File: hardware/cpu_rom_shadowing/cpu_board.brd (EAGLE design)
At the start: 167.9 x 122.5 mm, 53 parts, among them IC4 7404N, IC5 7400N, IC6 74HCT139N, IC7 7400N, IC9 74HCT138N, X1 22-23-2041

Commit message: ROM shadowed version of PCB modified
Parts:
- removed C15: 100n, rcl:C1206
- removed C5: 100n, rcl:C0603
- removed IC4: 7404N, 74xx-us:DIL14
- removed IC7: 7400N, 74xx-eu:DIL14
- IC5: value 7400N -> 74HCT08N
- moved C16 100.0 mm to (16.8, 107.7)
- moved IC5 92.7 mm to (118.7, 13.3), turned to 270 degrees
- moved C12 3.82 mm to (106.7, 23.5)
- moved IC6 3.19 mm to (99.7, 14.6)
- moved C17 1.27 mm to (78.7, 92.7)
- moved Q1 1.27 mm to (75.6, 94.0)
- moved C13 0.63 mm to (143.2, 23.5)
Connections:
- removed net A14_SWITCH: IC5.6, U$5.20
- removed net A15_SWITCH: IC5.3, U$5.7
- removed net BANK_A14: IC7.6, U$2.1
- removed net CS_BANKED_RAM: IC6.12, U$2.20
- removed net CS_RAM: IC6.4, U$4.20
- removed net N$19: IC6.15, IC6.5
- removed net N$20: IC9.6, R9.1
- removed net N$21: IC5.5, IC5.8
- removed net N$26: IC5.1, IC5.11
- removed net START_MEM_SWITCH: IC5.2, IC5.4, U$1.8
- new net CS_RAM1: IC6.10, U$4.20
- new net CS_RAM2: IC5.6, U$2.20
- new net N$2: IC5.4, IC6.11
- new net N$8: IC5.5, IC6.9
- new net PULLUP_5V: IC5.10, IC5.12, IC9.6, R9.1
- new net SHADOW_ROM: IC6.14, U$1.8
- net !CS_PORT_OUT: now also IC5.8; no longer IC4.8
- net !RESET: now also IC5.11; no longer IC4.4
- net 8275_DACK: no longer IC7.4
- net A14: now also U$2.1; no longer IC6.14
- net A14_CPU: now also U$5.20; no longer IC5.10, IC5.9
- net A15: now also IC6.13; no longer IC6.2
- net A15_CPU: now also U$5.7; no longer IC5.12, IC5.13
- net CS_EPROM: now also IC6.12; no longer IC6.11
- net CS_PORT_OUT: now also IC5.9; no longer IC4.9
- net GND: now also IC5.1, IC5.2, IC6.15, IC6.2; no longer C15.2, C5.2, IC4.1, IC4.11, IC4.13, IC4.5, IC4.7, IC6.13, IC7.1, IC7.10, IC7.12, IC7.13, IC7.2, IC7.7, IC7.9
- net RESET: now also IC5.13; no longer IC4.3
- net SET_BANK_A14: no longer IC7.5
- net VCC: no longer C15.1, C5.1, IC4.14, IC7.14
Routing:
- net START_MEM_SWITCH: track 188.3 -> 0.00 mm, vias 4 -> 0
- net VCC: track 624.8 -> 527.3 mm
- net SHADOW_ROM: track 0.00 -> 96.6 mm, vias 0 -> 2
- net BANK_A14: track 88.4 -> 0.00 mm, vias 4 -> 0
- net CS_RAM1: track 0.00 -> 87.4 mm, vias 0 -> 2
- net CS_BANKED_RAM: track 85.8 -> 0.00 mm, vias 2 -> 0
- net CS_RAM2: track 0.00 -> 79.3 mm, vias 0 -> 2
- net CS_RAM: track 76.4 -> 0.00 mm, vias 2 -> 0
- net A15_SWITCH: track 63.2 -> 0.00 mm, vias 2 -> 0
- net A14_SWITCH: track 55.0 -> 0.00 mm, vias 2 -> 0
- net A15_CPU: track 86.3 -> 37.2 mm, vias 2 -> 0
- net SET_BANK_A14: track 46.0 -> 0.00 mm, vias 2 -> 0
- net 8275_DACK: track 43.4 -> 0.00 mm
- net A14_CPU: track 45.7 -> 9.41 mm, vias 2 -> 0
- net PULLUP_5V: track 0.00 -> 31.1 mm
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
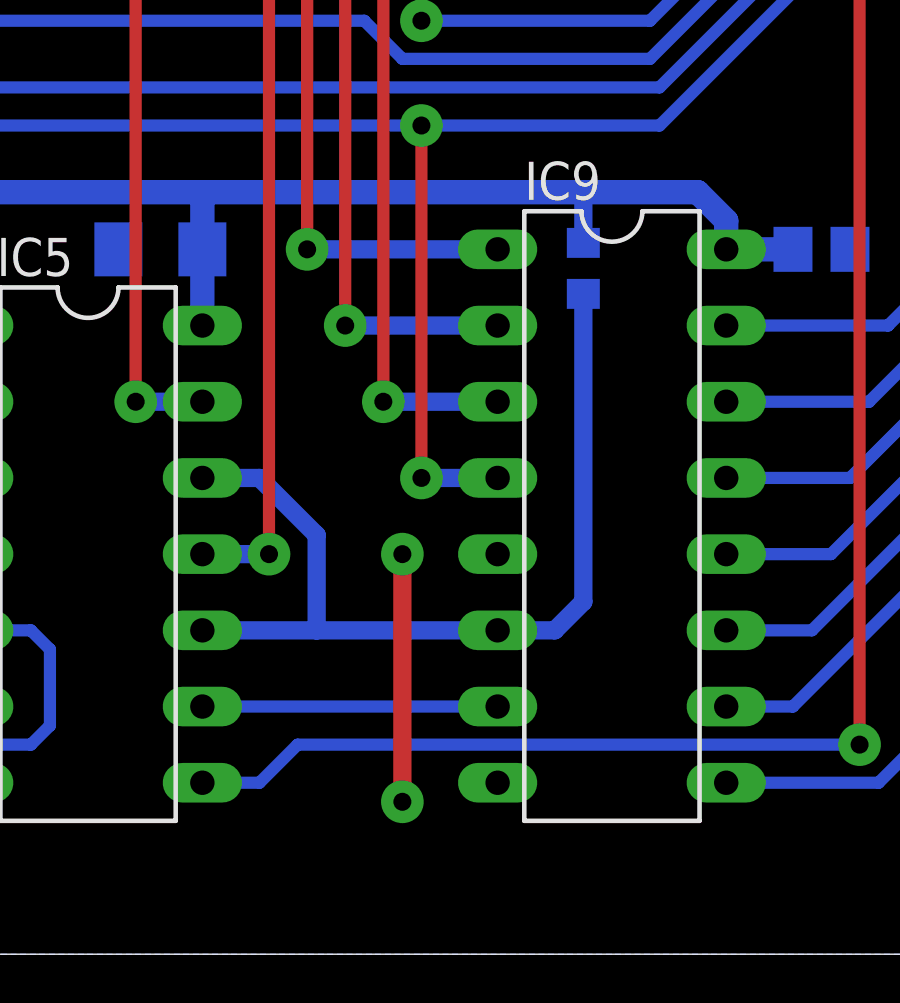
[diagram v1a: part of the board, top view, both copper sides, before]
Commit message: Isolate pramaeter changeg in CPU board
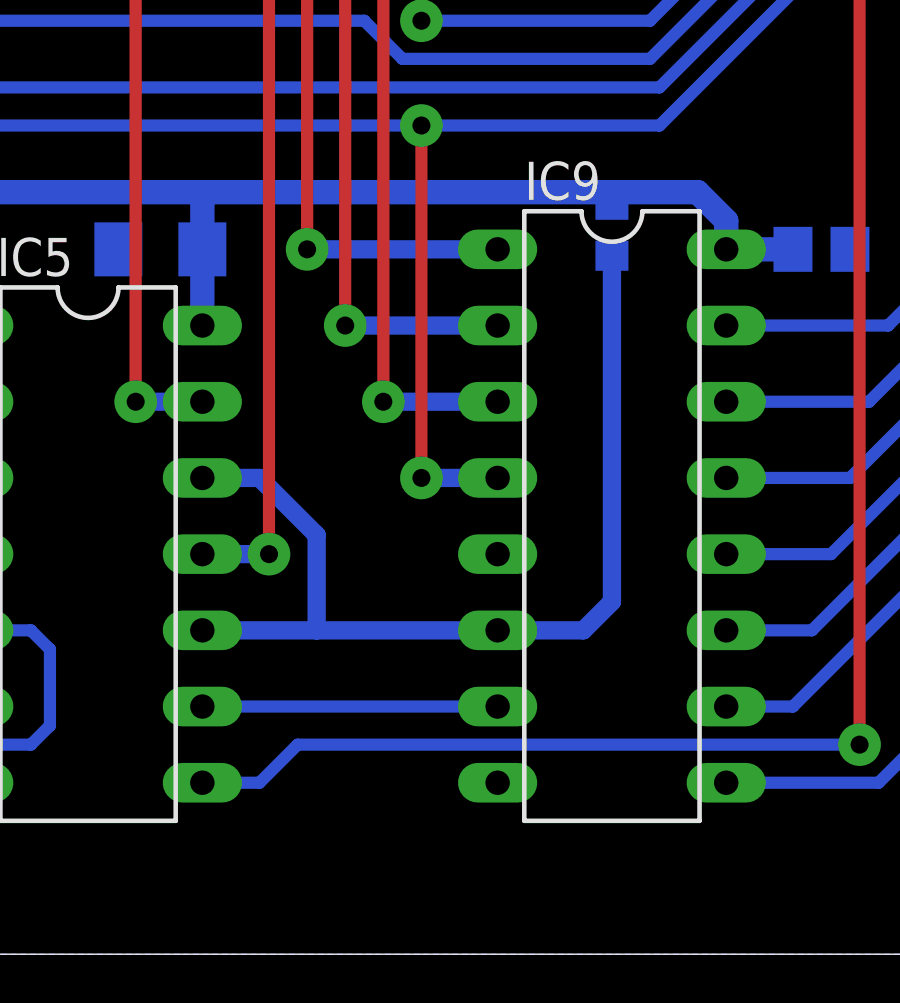
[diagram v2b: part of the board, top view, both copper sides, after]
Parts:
- moved R9 1.59 mm to (136.2, 24.1)
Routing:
- net GND: track 143.0 -> 134.8 mm, vias 18 -> 16
- net PULLUP_5V: track 31.1 -> 33.4 mm
- net VCC: track 527.3 -> 526.0 mm
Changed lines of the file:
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@@
 <element name="C9" library="rcl" package="C1206" value="100n" x="100.965" y="117.6147" rot="MR90"/>
 <element name="IC6" library="74xx-eu" package="DIL16" value="74HCT139N" x="99.695" y="14.605" rot="R270"/>
-<element name="R9" library="rcl" package="R0603" value="10k" x="135.255" y="22.86" rot="MR90"/>
+<element name="R9" library="rcl" package="R0603" value="10k" x="136.2075" y="24.13" rot="MR90"/>
 <element name="C10" library="rcl" package="E5-10,5" value="" x="134.62" y="113.665" rot="R270"/>
 <element name="C11" library="rcl" package="C0805" value="100n" x="48.5775" y="111.4425" rot="MR90"/>
@@
 <wire x1="93.345" y1="25.4" x2="103.505" y2="25.4" width="0.8128" layer="16"/>
 <wire x1="103.505" y1="25.4" x2="122.555" y2="25.4" width="0.8128" layer="16"/>
-<wire x1="122.555" y1="25.4" x2="135.255" y2="25.4" width="0.8128" layer="16"/>
-<wire x1="135.255" y1="25.4" x2="139.065" y2="25.4" width="0.8128" layer="16"/>
+<wire x1="122.555" y1="25.4" x2="136.2075" y2="25.4" width="0.8128" layer="16"/>
+<wire x1="136.2075" y1="25.4" x2="139.065" y2="25.4" width="0.8128" layer="16"/>
 <wire x1="139.065" y1="25.4" x2="140.0175" y2="24.4475" width="0.8128" layer="16"/>
 <wire x1="140.0175" y1="24.4475" x2="140.0175" y2="23.495" width="0.8128" layer="16"/>
-<wire x1="135.255" y1="23.71" x2="135.255" y2="25.4" width="0.6096" layer="16"/>
+<wire x1="136.2075" y1="24.98" x2="136.2075" y2="25.4" width="0.6096" layer="16"/>
 <wire x1="10.795" y1="71.755" x2="13.97" y2="71.755" width="0.6096" layer="16"/>
 <wire x1="13.97" y1="71.755" x2="18.7325" y2="71.755" width="0.6096" layer="16"/>
@@
 <wire x1="118.6434" y1="45.4884" x2="118.745" y2="45.4376" width="1.016" layer="16"/>
 <wire x1="118.7196" y1="45.463" x2="118.745" y2="45.4376" width="1.016" layer="16"/>
-<polygon width="0.4064" layer="16" isolate="0.6096" thermals="no">
+<polygon width="0.4064" layer="16" isolate="0.4064" thermals="no">
 <vertex x="0" y="122.555"/>
 <vertex x="0" y="0"/>
@@
 <contactref element="IC6" pad="3"/>
 <contactref element="IC6" pad="1"/>
-<via x="129.2225" y="13.335" extent="1-16" drill="0.6" diameter="1.4224" shape="octagon"/>
-<via x="129.2225" y="5.08" extent="1-16" drill="0.6" diameter="1.4224" shape="octagon"/>
-<wire x1="129.2225" y1="13.335" x2="129.2225" y2="5.08" width="0.6096" layer="1"/>
 <contactref element="IC5" pad="1"/>
 <contactref element="IC5" pad="2"/>
@@
 <contactref element="IC9" pad="6"/>
 <contactref element="R9" pad="1"/>
-<wire x1="135.255" y1="22.01" x2="135.255" y2="11.7475" width="0.6096" layer="16"/>
-<wire x1="135.255" y1="11.7475" x2="134.3025" y2="10.795" width="0.6096" layer="16"/>
-<wire x1="132.3975" y1="10.795" x2="134.3025" y2="10.795" width="0.6096" layer="16"/>
+<wire x1="136.2075" y1="23.28" x2="136.2075" y2="11.7475" width="0.6096" layer="16"/>
+<wire x1="136.2075" y1="11.7475" x2="135.255" y2="10.795" width="0.6096" layer="16"/>
+<wire x1="132.3975" y1="10.795" x2="135.255" y2="10.795" width="0.6096" layer="16"/>
 <contactref element="IC5" pad="10"/>
 <wire x1="122.555" y1="10.795" x2="126.365" y2="10.795" width="0.6096" layer="16"/>

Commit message: CPU board (ROM shadowing version) fix
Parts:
- IC5: value 74HCT08N -> 74LS86N; device 74xx-eu:DIL14 -> 74xx-us:DIL14
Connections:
- new net N$16: IC5.5, IC6.7
- net A15: now also IC6.14; no longer IC6.13
- net GND: no longer IC6.2, IC6.3
- net N$2: now also IC6.2; no longer IC5.4
- net N$8: now also IC6.3; no longer IC5.5
- net PULLUP_5V: now also IC5.4
- net SHADOW_ROM: now also IC6.13; no longer IC6.14
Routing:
- net N$16: track 0.00 -> 26.9 mm
- net PULLUP_5V: track 33.4 -> 42.0 mm
- net N$2: track 12.5 -> 15.9 mm
- net SHADOW_ROM: track 96.6 -> 99.1 mm
- net A15: track 195.0 -> 192.5 mm
- net N$8: track 20.1 -> 21.3 mm, vias 0 -> 2
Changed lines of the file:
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@@
 <attribute name="OC_FARNELL" value="unknown" x="156.845" y="56.515" size="1.778" layer="27" rot="R270" display="off"/>
 </element>
-<element name="IC5" library="74xx-eu" package="DIL14" value="74HCT08N" x="118.745" y="13.335" rot="R270"/>
+<element name="IC5" library="74xx-us" package="DIL14" value="74LS86N" x="118.745" y="13.335" rot="R270"/>
 </elements>
 <signals>
@@
 <wire x1="103.505" y1="103.505" x2="103.505" y2="101.73" width="0.8128" layer="16"/>
 <wire x1="113.665" y1="116.205" x2="134.62" y2="116.205" width="1.4224" layer="16"/>
-<contactref element="IC5" pad="14"/>
 <wire x1="122.555" y1="20.955" x2="122.555" y2="23.494540625" width="0.8128" layer="16"/>
 <wire x1="122.555" y1="23.494540625" x2="122.555459375" y2="23.495" width="0.8128" layer="16"/>
@@
 <wire x1="16.8275" y1="109.2214" x2="16.8275" y2="109.5375" width="1.016" layer="16"/>
 <wire x1="16.8275" y1="109.5375" x2="16.51" y2="109.855" width="1.016" layer="16"/>
+<contactref element="IC5" pad="14"/>
 </signal>
 <signal name="GND">
@@
 <contactref element="SV2" pad="56"/>
 <contactref element="SV2" pad="55"/>
-<contactref element="IC5" pad="7"/>
 <contactref element="IC6" pad="15"/>
-<contactref element="IC6" pad="2"/>
-<contactref element="IC6" pad="3"/>
 <contactref element="IC6" pad="1"/>
 <contactref element="IC5" pad="1"/>
 <contactref element="IC5" pad="2"/>
+<contactref element="IC5" pad="7"/>
 </signal>
 <signal name="D0">
@@
 <wire x1="108.585" y1="42.545" x2="24.4475" y2="42.545" width="0.4064" layer="16"/>
 <contactref element="SV2" pad="30"/>
-<via x="108.585" y="15.875" extent="1-16" drill="0.6" diameter="1.4224" shape="octagon"/>
-<wire x1="108.585" y1="15.875" x2="108.585" y2="42.545" width="0.4064" layer="1"/>
+<via x="108.585" y="18.415" extent="1-16" drill="0.6" diameter="1.4224" shape="octagon"/>
+<wire x1="108.585" y1="18.415" x2="108.585" y2="42.545" width="0.4064" layer="1"/>
 <via x="108.585" y="42.545" extent="1-16" drill="0.6" diameter="1.4224" shape="octagon"/>
-<contactref element="IC6" pad="13"/>
-<wire x1="108.585" y1="15.875" x2="103.505" y2="15.875" width="0.4064" layer="16"/>
+<contactref element="IC6" pad="14"/>
+<wire x1="103.505" y1="18.415" x2="108.585" y2="18.415" width="0.6096" layer="16"/>
 </signal>
 <signal name="A13">
@@
 <wire x1="124.46" y1="15.875" x2="126.365" y2="13.97" width="0.6096" layer="16"/>
 <wire x1="126.365" y1="13.97" x2="126.365" y2="10.795" width="0.6096" layer="16"/>
+<contactref element="IC5" pad="4"/>
+<wire x1="114.935" y1="13.335" x2="118.745" y2="13.335" width="0.6096" layer="16"/>
+<wire x1="118.745" y1="13.335" x2="121.285" y2="10.795" width="0.6096" layer="16"/>
+<wire x1="121.285" y1="10.795" x2="122.555" y2="10.795" width="0.6096" layer="16"/>
 </signal>
 <signal name="CS_PORT_OUT">
@@
 <signal name="SHADOW_ROM">
 <contactref element="U$1" pad="8"/>
-<contactref element="IC6" pad="14"/>
 <wire x1="118.745" y1="92.71" x2="118.745" y2="95.885" width="0.4064" layer="16"/>
 <wire x1="118.745" y1="95.885" x2="117.475" y2="97.155" width="0.4064" layer="16"/>
@@
 <wire x1="107.315" y1="95.25" x2="107.315" y2="89.535" width="0.4064" layer="16"/>
 <via x="107.315" y="89.535" extent="1-16" drill="0.6" diameter="1.4224" shape="octagon"/>
-<wire x1="107.315" y1="89.535" x2="107.315" y2="18.415" width="0.4064" layer="1"/>
-<via x="107.315" y="18.415" extent="1-16" drill="0.6" diameter="1.4224" shape="octagon"/>
-<wire x1="103.505" y1="18.415" x2="107.315" y2="18.415" width="0.6096" layer="16"/>
+<wire x1="107.315" y1="89.535" x2="107.315" y2="15.875" width="0.4064" layer="1"/>
+<via x="107.315" y="15.875" extent="1-16" drill="0.6" diameter="1.4224" shape="octagon"/>
+<contactref element="IC6" pad="13"/>
+<wire x1="103.505" y1="15.875" x2="107.315" y2="15.875" width="0.6096" layer="16"/>
 </signal>
 <signal name="N$2">
 <contactref element="IC6" pad="11"/>
-<contactref element="IC5" pad="4"/>
-<wire x1="103.505" y1="10.795" x2="111.4425" y2="10.795" width="0.4064" layer="16"/>
-<wire x1="111.4425" y1="10.795" x2="113.9825" y2="13.335" width="0.4064" layer="16"/>
-<wire x1="113.9825" y1="13.335" x2="114.935" y2="13.335" width="0.4064" layer="16"/>
+<contactref element="IC6" pad="2"/>
+<wire x1="95.885" y1="20.955" x2="98.425" y2="20.955" width="0.4064" layer="16"/>
+<wire x1="98.425" y1="20.955" x2="100.33" y2="19.05" width="0.4064" layer="16"/>
+<wire x1="100.33" y1="19.05" x2="100.33" y2="12.065" width="0.4064" layer="16"/>
+<wire x1="100.33" y1="12.065" x2="101.6" y2="10.795" width="0.4064" layer="16"/>
+<wire x1="101.6" y1="10.795" x2="103.505" y2="10.795" width="0.4064" layer="16"/>
 </signal>
 <signal name="N$8">
 <contactref element="IC6" pad="9"/>
+<wire x1="103.505" y1="5.715" x2="104.4575" y2="5.715" width="0.4064" layer="16"/>
+<contactref element="IC6" pad="3"/>
+<wire x1="103.505" y1="5.715" x2="99.06" y2="5.715" width="0.6096" layer="16"/>
+<via x="99.06" y="5.715" extent="1-16" drill="0.6" diameter="1.4224" shape="octagon"/>
+<wire x1="99.06" y1="5.715" x2="99.06" y2="18.415" width="0.4064" layer="1"/>
+<via x="99.06" y="18.415" extent="1-16" drill="0.6" diameter="1.4224" shape="octagon"/>
+<wire x1="99.06" y1="18.415" x2="95.885" y2="18.415" width="0.6096" layer="16"/>
+</signal>
+<signal name="N$16">
 <contactref element="IC5" pad="5"/>
-<wire x1="103.505" y1="5.715" x2="104.4575" y2="5.715" width="0.4064" layer="16"/>
-<wire x1="116.84" y1="6.985" x2="117.475" y2="7.62" width="0.4064" layer="16"/>
-<wire x1="117.475" y1="7.62" x2="117.475" y2="10.16" width="0.4064" layer="16"/>
-<wire x1="117.475" y1="10.16" x2="116.84" y2="10.795" width="0.4064" layer="16"/>
-<wire x1="116.84" y1="10.795" x2="114.935" y2="10.795" width="0.4064" layer="16"/>
-<wire x1="116.84" y1="6.985" x2="105.7275" y2="6.985" width="0.4064" layer="16"/>
-<wire x1="105.7275" y1="6.985" x2="104.4575" y2="5.715" width="0.4064" layer="16"/>
+<contactref element="IC6" pad="7"/>
+<wire x1="95.885" y1="8.255" x2="97.155" y2="8.255" width="0.4064" layer="16"/>
+<wire x1="97.155" y1="8.255" x2="98.425" y2="6.985" width="0.4064" layer="16"/>
+<wire x1="98.425" y1="6.985" x2="116.5225" y2="6.985" width="0.4064" layer="16"/>
+<wire x1="116.5225" y1="6.985" x2="117.1575" y2="7.62" width="0.4064" layer="16"/>
+<wire x1="117.1575" y1="7.62" x2="117.1575" y2="9.8425" width="0.4064" layer="16"/>
+<wire x1="117.1575" y1="9.8425" x2="116.205" y2="10.795" width="0.4064" layer="16"/>
+<wire x1="116.205" y1="10.795" x2="114.935" y2="10.795" width="0.4064" layer="16"/>
 </signal>
 </signals>
